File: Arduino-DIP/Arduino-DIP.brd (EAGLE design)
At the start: 55.9 x 22.9 mm, 16 parts, among them IC1 ATMEGA 328, IC2 MCP1702-33, X1 16 MHz

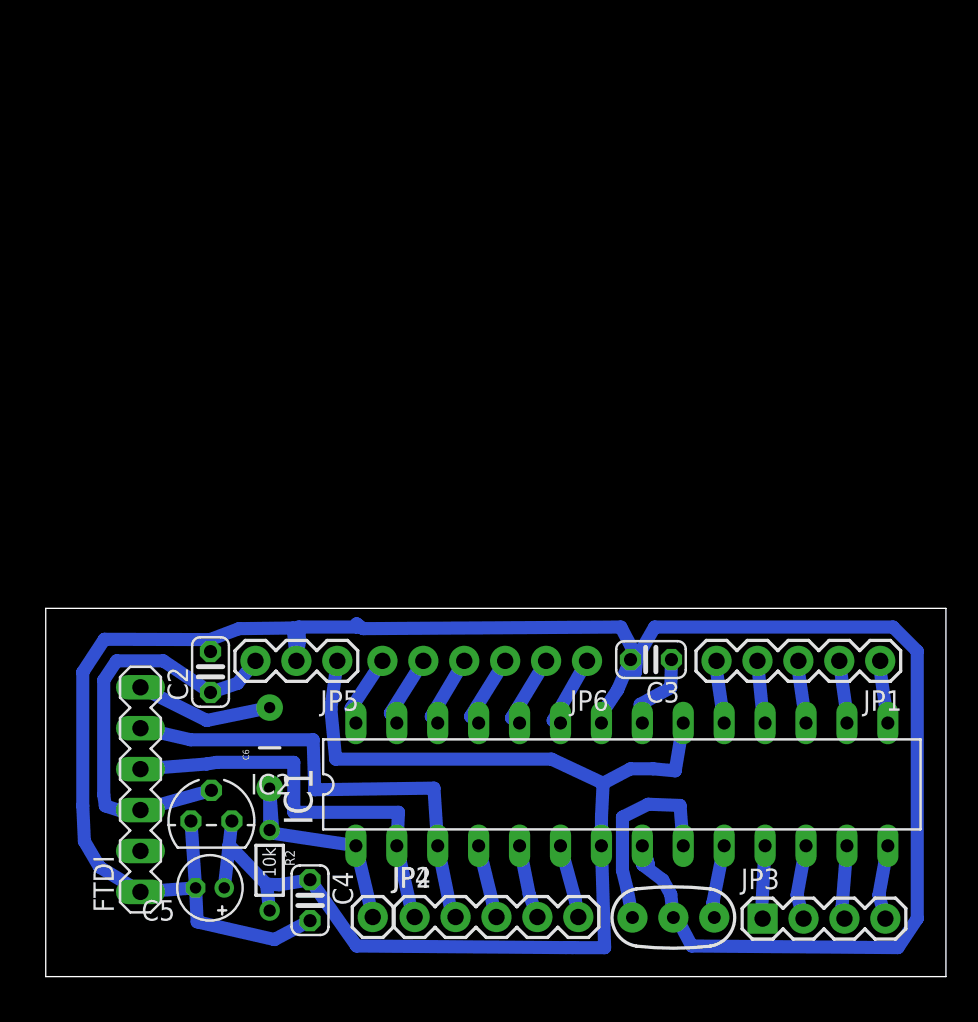
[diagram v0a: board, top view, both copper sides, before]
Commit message: finished routing DIP board and added tool patch for 1/32
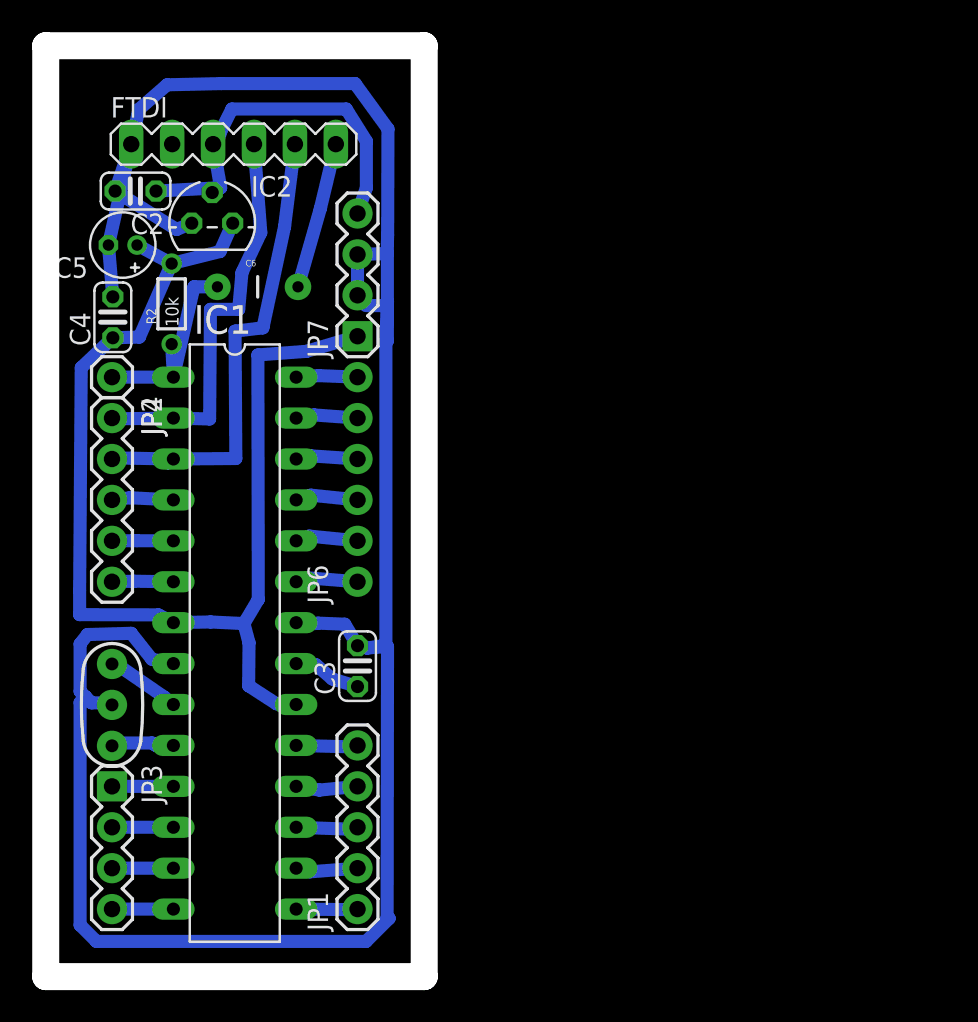
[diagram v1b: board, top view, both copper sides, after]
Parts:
- removed JP5: (no value), SparkFun-Connectors:1X03
- added JP7: (no value), SparkFun-Connectors:1X04
- moved JP3 41.2 mm to (4.11, 11.8), turned to 270 degrees
- moved FTDI 40.5 mm to (11.7, 51.7), turned to 0 degrees
- moved C5 40.3 mm to (4.78, 45.4)
- moved C4 38.2 mm to (4.17, 40.9), turned to 90 degrees
- moved X1 37.3 mm to (4.11, 16.9), turned to 270 degrees
- moved JP4 37.2 mm to (4.11, 37.2), turned to 270 degrees
- moved IC2 37.1 mm to (10.3, 46.8)
- moved JP2 36.2 mm to (4.11, 34.7), turned to 270 degrees
- moved JP1 35.9 mm to (19.4, 4.19), turned to 90 degrees
- moved R2 35.7 mm to (7.82, 41.8), turned to 90 degrees
- moved C2 30.2 mm to (5.58, 48.8), turned to 180 degrees
- moved C6 28.6 mm to (13.2, 42.8), turned to 0 degrees
- moved IC1 25.6 mm to (11.7, 20.7), turned to 270 degrees
- moved C3 18.2 mm to (19.4, 19.3), turned to 90 degrees
- moved JP6 15.1 mm to (19.4, 24.5), turned to 90 degrees
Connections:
- net GND: now also JP7.2, JP7.3; no longer JP5.2
- net PWR: now also JP7.4; no longer JP5.3
- net VCC: now also JP7.1; no longer JP5.1
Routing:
- net GND: track 142.1 -> 149.7 mm
- net N$1: track 12.6 -> 5.03 mm
- net RST: track 15.2 -> 13.1 mm
- net PWR: track 26.1 -> 24.5 mm
- net TXD: track 30.3 -> 29.4 mm
- net N$19: track 5.17 -> 4.22 mm
- net N$3: track 4.73 -> 3.88 mm
- net N$4: track 4.71 -> 3.87 mm
- net N$14: track 4.63 -> 3.81 mm
- net N$12: track 4.63 -> 3.81 mm
- net N$2: track 4.78 -> 3.98 mm
- net N$9: track 4.57 -> 3.81 mm
- net N$10: track 4.56 -> 3.81 mm
- net N$5: track 4.58 -> 3.84 mm
- net N$13: track 4.55 -> 3.81 mm
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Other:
- board size 55.9 x 22.9 mm -> 23.5 x 57.8 mm
- board text added: "D13 D12 D11 D10 D9"
- board text added: "D5 D6 D7 D8"
- board text added: "RESET D0 D1 D2 D3 D4"
- board text added: "Vin GND GND Vcc A5 A4 A3 A2 A1 A0"
